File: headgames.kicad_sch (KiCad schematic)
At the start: 49 parts, among them J1 9V BATTERY IN, J2 ELECTRODES, U1 LM358N INVENTORY, U2 LM324N INVENTORY, U3 LM386

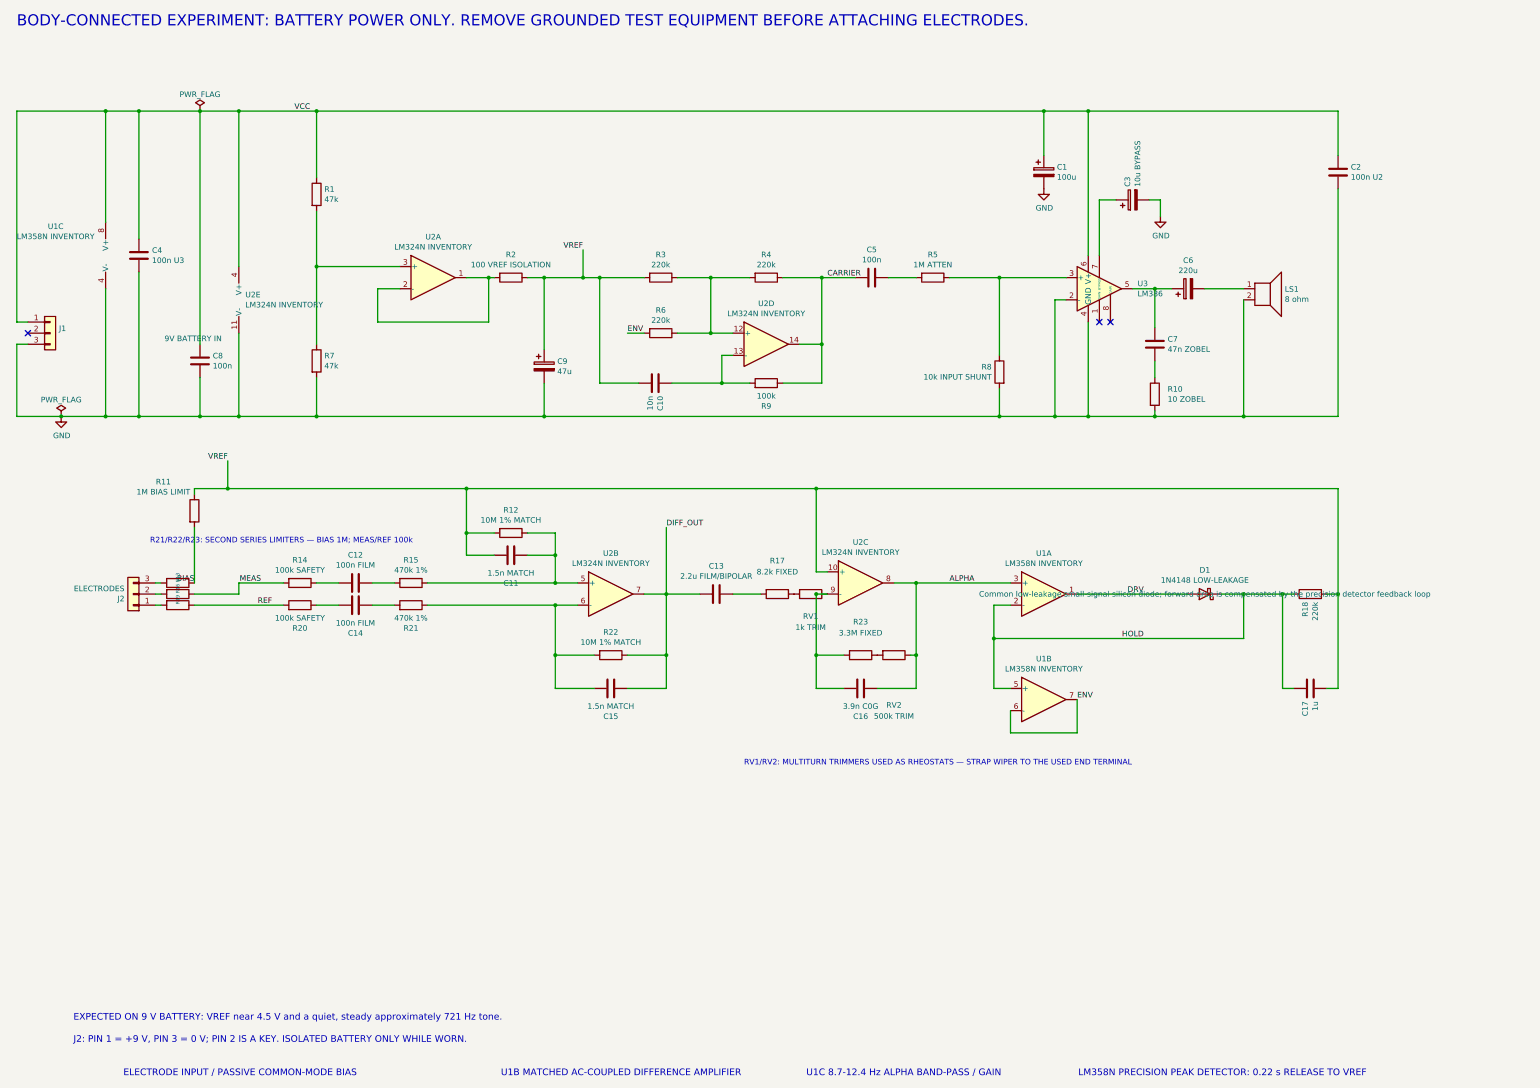
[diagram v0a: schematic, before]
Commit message: Reconcile KiCad with direct end-to-end sonification path
Replace the historical LM358/1N4148 peak-detector path in the authoritative schematic with the physical path exercised by the speaker-current simulation. Repurpose the stocked LM358N as independent electrode-site MEAS and REF unity-gain buffers, preserve both redundant 100 kohm electrode safety resistors ahead of each buffer, and drive the acquisition inputs through independent selected 8.2 kohm cable-isolation resistors.

Connect the ALPHA output directly and bipolarly to the U2D relaxation oscillator through R6, retaining the existing gain-20 LM386 input attenuation, output coupling, speaker load, and Zobel network. Document the five-conductor active-assembly boundary as buffered MEAS, buffered REF, BIAS, isolated VCC, and isolated return, and remove obsolete envelope/hold drawing artifacts and annotations.

Replace the hard-coded mismatch audit with exact native-netlist assertions for both active followers, both isolation resistors, direct ALPHA control, acquisition, oscillator, and speaker-current blocks. Retire detector-centered checks from the gating root regression and make acceptance execute the nominal noisy wet/alpha endpoint experiment after topology alignment.

Update the project guidance and README to invalidate stale proxy-frontier selections, record the current 16-phase nominal alpha-modulation failure, and distinguish schematic reconciliation from model acceptance.

Verified with KiCad 9.0.9 ERC at zero violations, the Typer root regression suite, exact KiCad/model boundary comparison, and an intentional acceptance failure at the actual nominal alpha-modulation gate.
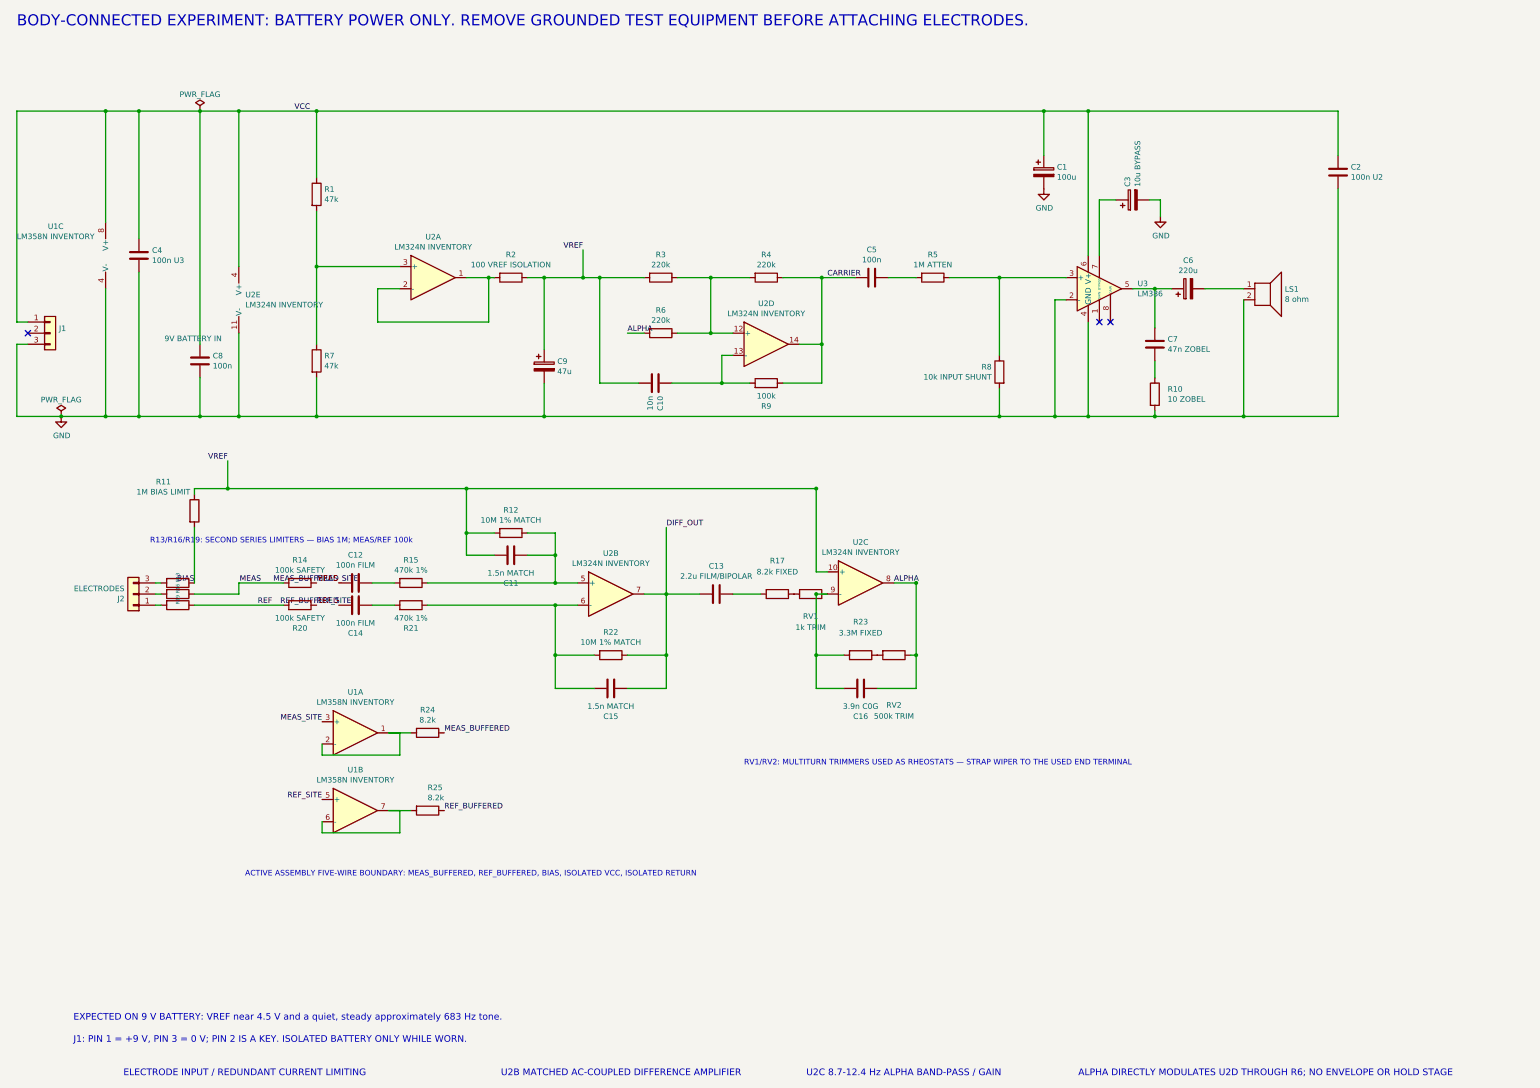
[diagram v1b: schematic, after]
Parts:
- removed C17: 1u, symbol Device:C
- R24: renamed from D1; value 1N4148 LOW-LEAKAGE -> 8.2k; symbol Device:D_Schottky -> Device:R
- R25: renamed from R18; value 220k -> 8.2k
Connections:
- net ALPHA: now also R6.2; no longer U1.3 (+)
- net VREF: no longer R25.2
- net MEAS_BUFFERED: now reaches C12.2
- net MEAS_BUFFERED: now also R24.1; no longer R14.1
- net REF_BUFFERED: now reaches C14.2
- net REF_BUFFERED: now also R25.1; no longer R20.1
- net DRV: no longer names the net of R24.2, U1.1
- net DRV: now also U1.2 (-)
- net ENV: no longer names the net of U1.6 (-), U1.7
- net ENV: now also R25.2; no longer R6.2
- removed net HOLD: R24.1 (K), R25.1, U1.2 (-), U1.5 (+)
- new net MEAS_SITE: R14.1, U1.3 (+)
- new net REF_SITE: R20.1, U1.5 (+)
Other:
- note added: "ACTIVE ASSEMBLY FIVE-WIRE BOUNDARY: MEAS_BUFFERED, REF_BUFFERED, BIAS, ISOLATED VCC, ISOLATED RETURN"
- note added: "ALPHA DIRECTLY MODULATES U2D THROUGH R6; NO ENVELOPE OR HOLD STAGE"
- note added: "ELECTRODE INPUT / REDUNDANT CURRENT LIMITING"
- note added: "EXPECTED ON 9 V BATTERY: VREF near 4.5 V and a quiet, steady approximately 683 Hz tone."
- note added: "J1: PIN 1 = +9 V, PIN 3 = 0 V; PIN 2 IS A KEY. ISOLATED BATTERY ONLY WHILE WORN."
- note added: "R13/R16/R19: SECOND SERIES LIMITERS — BIAS 1M; MEAS/REF 100k"
- note added: "U2B MATCHED AC-COUPLED DIFFERENCE AMPLIFIER"
- note added: "U2C 8.7-12.4 Hz ALPHA BAND-PASS / GAIN"
- note removed: "ELECTRODE INPUT / PASSIVE COMMON-MODE BIAS"
- note removed: "EXPECTED ON 9 V BATTERY: VREF near 4.5 V and a quiet, steady approximately 721 Hz tone."
- note removed: "J2: PIN 1 = +9 V, PIN 3 = 0 V; PIN 2 IS A KEY. ISOLATED BATTERY ONLY WHILE WORN."
- note removed: "LM358N PRECISION PEAK DETECTOR: 0.22 s RELEASE TO VREF"
- note removed: "R21/R22/R23: SECOND SERIES LIMITERS — BIAS 1M; MEAS/REF 100k"
- note removed: "U1B MATCHED AC-COUPLED DIFFERENCE AMPLIFIER"
- note removed: "U1C 8.7-12.4 Hz ALPHA BAND-PASS / GAIN"
- moved on the sheet: R25, U1A, U1B

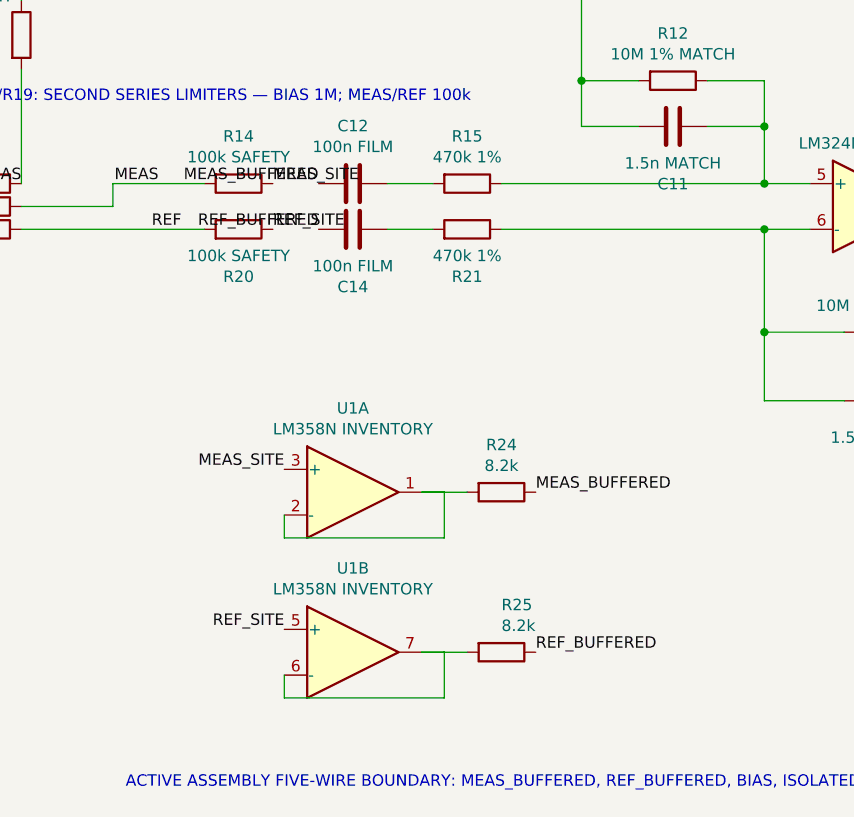
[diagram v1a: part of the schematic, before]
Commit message: Draw the active-electrode signal path explicitly
Replace the MEAS_SITE, REF_SITE, MEAS_BUFFERED, and REF_BUFFERED same-sheet label jumps with continuous native KiCad wire segments. This makes both redundant input-limiter chains, LM358 followers, 8.2 kohm isolation resistors, and acquisition inputs traceable directly on the drawing instead of relying on net-label semantics that resemble open stubs.

Add a root manage.py regression that rejects reintroduction of hidden label jumps on these safety-critical nets. Record explicit MEAS/REF continuity as an architectural invariant in AGENTS.md.

Verification: kicad-cli ERC completed with 0 errors and 0 warnings; UV_CACHE_DIR=.uv-cache uv run python manage.py test passed; a fresh 3200-pixel schematic render was visually inspected; git diff --check passed.
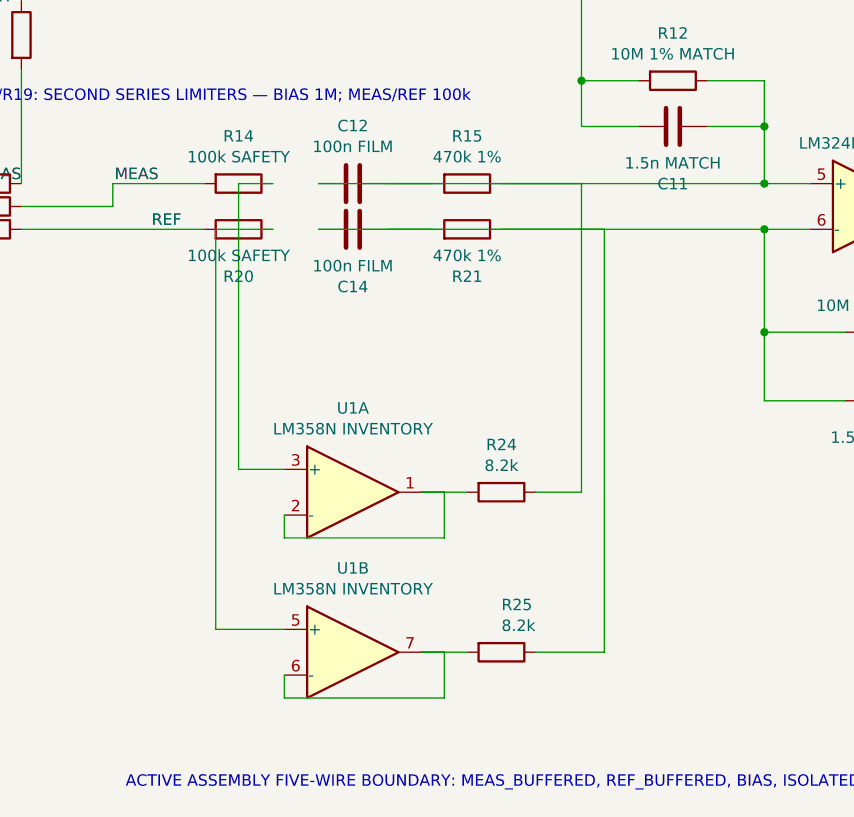
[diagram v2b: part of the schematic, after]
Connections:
- net MEAS_BUFFERED is gone; now on an unnamed net: C12.2, R24.1
- net REF_BUFFERED is gone; now on an unnamed net: C14.2, R25.1
- net at C12.1, R15.2: now also C11.1, R12.1, R15.1, U2.5 (+)
- net at C14.1, R21.2: now also C15.2, R21.1, R22.2, U2.6 (-)
- net MEAS_SITE: no longer names the net of R14.1, U1.3 (+)
- net REF_SITE: no longer names the net of R20.1, U1.5 (+)
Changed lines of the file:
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@@
 		(stroke (width 0) (type default))
 	)
-	(label "MEAS_SITE"
-		(at 87.63 177.8 180)
-		(effects (font (size 1.27 1.27)) (justify right bottom))
+	(wire
+		(pts
+			(xy 86.36 146.05) (xy 82.55 146.05)
+		)
+		(stroke (width 0) (type default))
 	)
-	(label "MEAS_SITE"
-		(at 86.36 146.05 0)
-		(effects (font (size 1.27 1.27)) (justify left bottom))
+	(wire
+		(pts
+			(xy 82.55 146.05) (xy 82.55 177.8)
+		)
+		(stroke (width 0) (type default))
 	)
-	(label "MEAS_BUFFERED"
-		(at 115.57 180.34 0)
-		(effects (font (size 1.27 1.27)) (justify left bottom))
+	(wire
+		(pts
+			(xy 82.55 177.8) (xy 87.63 177.8)
+		)
+		(stroke (width 0) (type default))
 	)
-	(label "MEAS_BUFFERED"
-		(at 91.44 146.05 180)
-		(effects (font (size 1.27 1.27)) (justify right bottom))
+	(wire
+		(pts
+			(xy 115.57 180.34) (xy 120.65 180.34)
+		)
+		(stroke (width 0) (type default))
 	)
-	(label "REF_SITE"
-		(at 87.63 195.58 180)
-		(effects (font (size 1.27 1.27)) (justify right bottom))
+	(wire
+		(pts (xy 120.65 180.34) (xy 120.65 146.05))
+		(stroke (width 0) (type default))
 	)
-	(label "REF_SITE"
-		(at 86.36 151.13 0)
-		(effects (font (size 1.27 1.27)) (justify left bottom))
+	(wire
+		(pts (xy 120.65 146.05) (xy 91.44 146.05))
+		(stroke (width 0) (type default))
 	)
-	(label "REF_BUFFERED"
-		(at 115.57 198.12 0)
-		(effects (font (size 1.27 1.27)) (justify left bottom))
+	(wire
+		(pts (xy 86.36 151.13) (xy 80.01 151.13))
+		(stroke (width 0) (type default))
 	)
-	(label "REF_BUFFERED"
-		(at 91.44 151.13 180)
-		(effects (font (size 1.27 1.27)) (justify right bottom))
+	(wire
+		(pts (xy 80.01 151.13) (xy 80.01 195.58))
+		(stroke (width 0) (type default))
+	)
+	(wire
+		(pts (xy 80.01 195.58) (xy 87.63 195.58))
+		(stroke (width 0) (type default))
+	)
+	(wire
+		(pts (xy 115.57 198.12) (xy 123.19 198.12))
+		(stroke (width 0) (type default))
+	)
+	(wire
+		(pts (xy 123.19 198.12) (xy 123.19 151.13))
+		(stroke (width 0) (type default))
+	)
+	(wire
+		(pts (xy 123.19 151.13) (xy 91.44 151.13))
+		(stroke (width 0) (type default))
 	)
 	(label "REF"

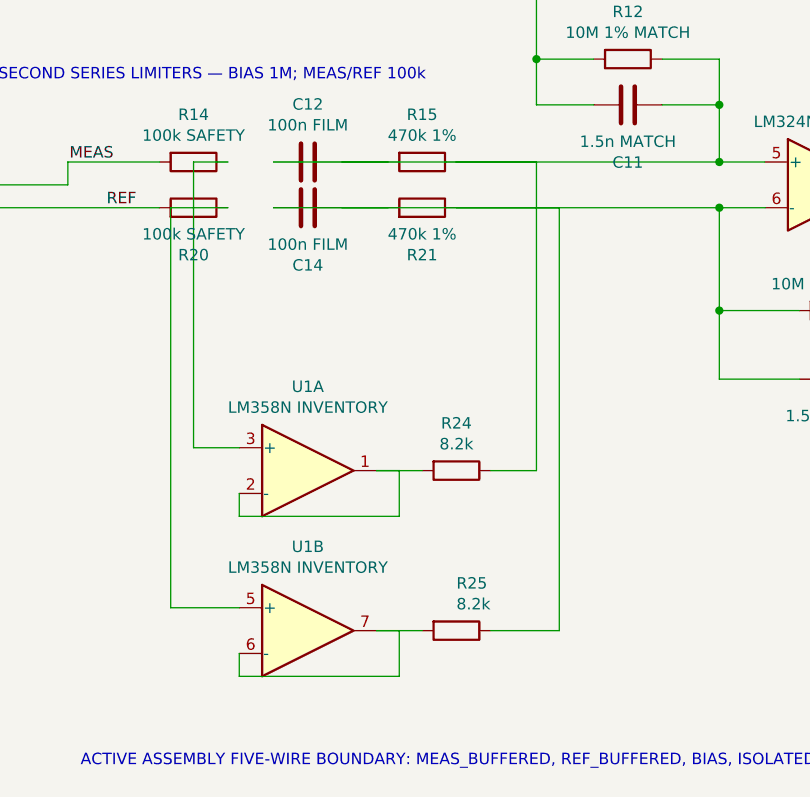
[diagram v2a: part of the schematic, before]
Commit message: Make both LM358 follower connections electrically explicit
Remove the duplicate overlapping output wires at U1A and U1B. Split each output conductor at its feedback branch so the output pin, isolation resistor, and inverting-input return meet at the same literal wire endpoint, with an explicit junction. This avoids relying on KiCad's ambiguous endpoint-on-overlap behavior.

Reroute the MEAS_BUFFERED and REF_BUFFERED returns so they no longer overlay the existing acquisition-stage conductors. The revised drawing keeps the core path continuous while avoiding positive-length collinear overlaps.

Add a root-level schematic geometry regression that scans every native KiCad wire segment and rejects duplicate or partially overlapping collinear interiors while permitting ordinary shared endpoints. This catches the U1 defect and the additional acquisition-wire overlays that the prior netlist-only assertions and ERC missed.

Verification: kicad-cli ERC reported 0 violations; the exported-net topology assertions prove U1 pins 1/2/R24 and pins 6/7/R25 share their intended nets; UV_CACHE_DIR=.uv-cache uv run python manage.py test passed including the new whole-schematic overlap gate; a fresh 3200-pixel render was visually inspected; git diff --check passed.
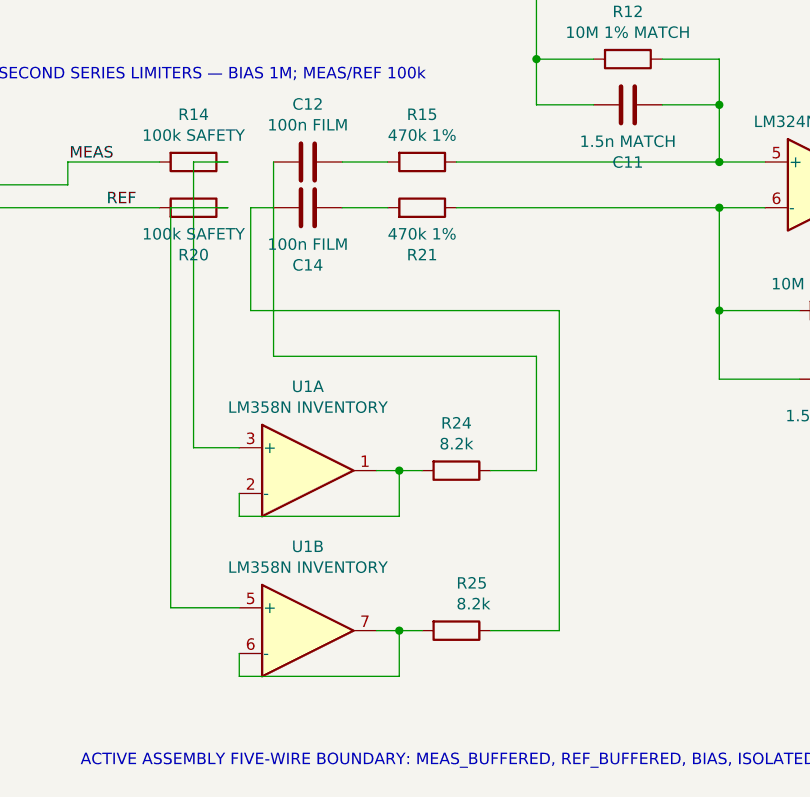
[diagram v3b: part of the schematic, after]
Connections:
- net at C11.1, R12.1, R15.1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: no longer C12.1, C12.2, R15.2, R24.1
- net at C15.2, R21.1, R22.2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: no longer C14.1, C14.2, R21.2, R25.1
- new net: C12.1, R15.2
- new net: C12.2, R24.1
- new net: C14.1, R21.2
- new net: C14.2, R25.1
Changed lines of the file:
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@@
+	)
+	(junction
+		(at 105.41 180.34)
+		(diameter 0)
+		(color 0 0 0 0)
+	)
+	(junction
+		(at 105.41 198.12)
+		(diameter 0)
+		(color 0 0 0 0)
 	)
 	(junction
@@
 	(wire
 		(pts
-			(xy 102.87 180.34) (xy 107.95 180.34)
-		)
-		(stroke (width 0) (type default))
-	)
-	(wire
-		(pts
 			(xy 102.87 180.34) (xy 105.41 180.34)
 		)
@@
 	(wire
 		(pts
-			(xy 102.87 198.12) (xy 107.95 198.12)
-		)
-		(stroke (width 0) (type default))
-	)
-	(wire
-		(pts
 			(xy 102.87 198.12) (xy 105.41 198.12)
 		)
@@
 	(wire
 		(pts
+			(xy 105.41 180.34) (xy 107.95 180.34)
+		)
+		(stroke (width 0) (type default))
+	)
+	(wire
+		(pts
+			(xy 105.41 198.12) (xy 107.95 198.12)
+		)
+		(stroke (width 0) (type default))
+	)
+	(wire
+		(pts
 			(xy 105.41 198.12) (xy 105.41 203.2)
 		)
@@
 	)
 	(wire
-		(pts (xy 120.65 180.34) (xy 120.65 146.05))
-		(stroke (width 0) (type default))
-	)
-	(wire
-		(pts (xy 120.65 146.05) (xy 91.44 146.05))
+		(pts (xy 120.65 180.34) (xy 120.65 167.64))
+		(stroke (width 0) (type default))
+	)
+	(wire
+		(pts (xy 120.65 167.64) (xy 91.44 167.64))
+		(stroke (width 0) (type default))
+	)
+	(wire
+		(pts (xy 91.44 167.64) (xy 91.44 146.05))
 		(stroke (width 0) (type default))
 	)
@@
 	)
 	(wire
-		(pts (xy 123.19 198.12) (xy 123.19 151.13))
-		(stroke (width 0) (type default))
-	)
-	(wire
-		(pts (xy 123.19 151.13) (xy 91.44 151.13))
-		(stroke (width 0) (type default))
-	)
+		(pts (xy 123.19 198.12) (xy 123.19 162.56))
+		(stroke (width 0) (type default))
+	)
+	(wire
+		(pts (xy 123.19 162.56) (xy 88.9 162.56))
+		(stroke (width 0) (type default))
+	)
+	(wire
+		(pts (xy 88.9 162.56) (xy 88.9 151.13))
+		(stroke (width 0) (type default))
+	)
+	(wire
+		(pts (xy 88.9 151.13) (xy 91.44 151.13))
+		(stroke (width 0) (type default))
+	)

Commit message: cleanup
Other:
- moved on the sheet: C1, C11, C12, C13, C14, C15, C16, C2, J2, R11, R12, R13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
